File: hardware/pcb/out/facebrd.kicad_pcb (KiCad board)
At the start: 2 copper layers, 56 x 68 mm, 33 parts, among them J1 ToF 4P, J2 MIC pads, J3 EYES 6P, J4 BAT, J5 LED 3P, J6 AMP 5P, J7 TOUCH pads, J8 CHG, U1 XIAO-ESP32S3, U2 MPR121QR2, U3 MPU-6050

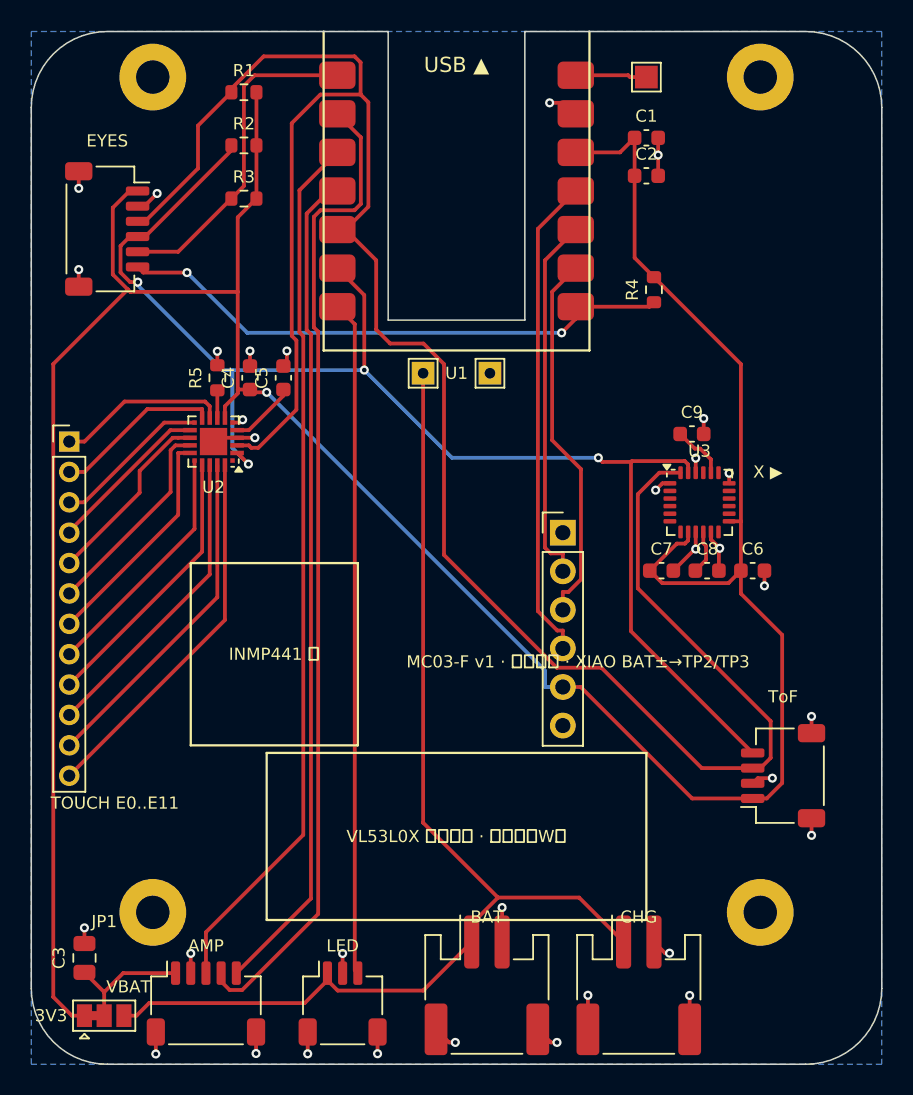
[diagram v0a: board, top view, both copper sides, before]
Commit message: pcb: correct MPR121 footprint (QFN-20 3x3 0.5 mm, 5 leads/side, no corner leads); local GND pour at U2
Co-Authored-By: Claude Fable 5.1 <noreply@anthropic.com>
Claude-Session: https://claude.ai/code/session_01F351BE8WNbsDJxZJegnrAN
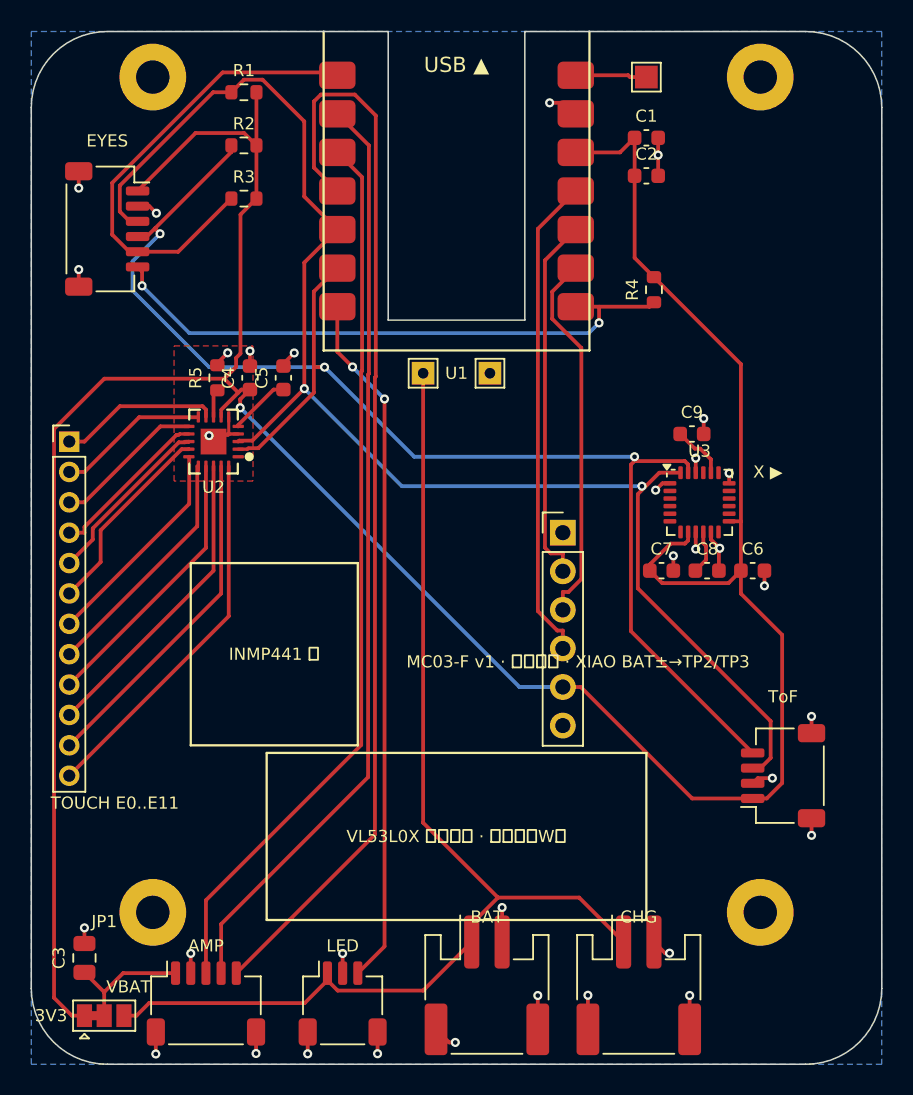
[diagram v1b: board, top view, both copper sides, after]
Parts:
- U2: footprint SiliconLabs_QFN-20-1EP_3x3mm_P0.5mm_EP1.8x1.8mm -> MC03:QFN-20_3x3_P0.5_MPR121
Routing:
- net SDA0: track 140.2 -> 95.5 mm, vias 0 -> 2
- net I2S_DIN: track 54.8 -> 71.6 mm
- net SDA1: track 21.8 -> 31.1 mm
- net I2S_LRC: track 65.3 -> 61.5 mm
- net SCL1: track 37.1 -> 39.4 mm
- net 3V3: track 198.9 -> 196.8 mm
- net SCL0: track 92.9 -> 94.6 mm, vias 4 -> 3
- net LED_DIN: track 44.4 -> 45.9 mm, vias 0 -> 2
- net I2S_BCLK: track 57.8 -> 59.0 mm
- net ELE1: track 11.1 -> 10.0 mm
- net GND: track 50.1 -> 49.3 mm
- net ELE0: track 11.2 -> 10.5 mm
- net ELE6: track 15.0 -> 14.3 mm
- net ELE4: track 12.2 -> 11.6 mm
- net ELE5: track 13.6 -> 13.0 mm
- added copper zone on F.Cu, net GND

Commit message: pcb: MPR121 pin map corrected against datasheet/KiCad symbol (7 REXT, 8-19 ELE, 20 VDD); MPU RESV pins NC; EP without paste
Co-Authored-By: Claude Fable 5.1 <noreply@anthropic.com>
Claude-Session: https://claude.ai/code/session_01F351BE8WNbsDJxZJegnrAN
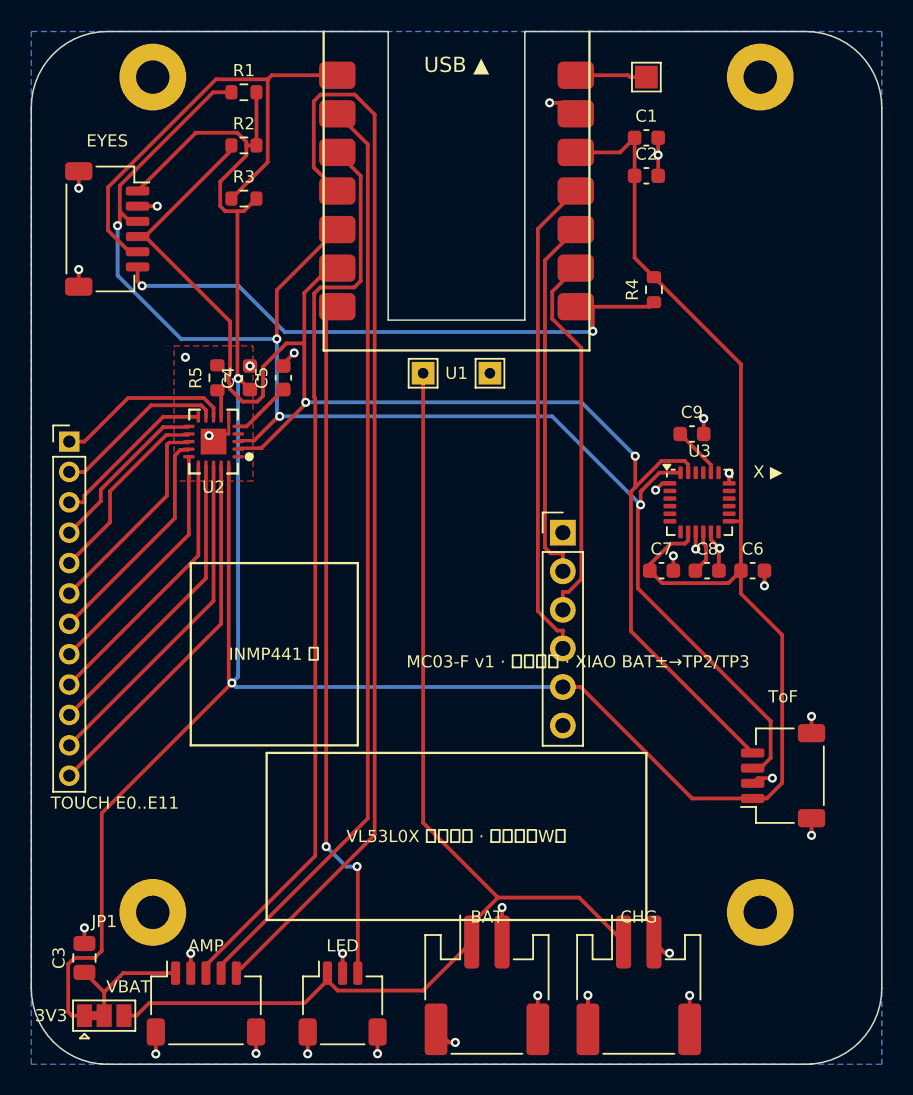
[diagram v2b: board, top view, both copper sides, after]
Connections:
- U2 pad 10: ELE1 -> ELE2
- U2 pad 11: ELE2 -> ELE3
- U2 pad 12: ELE3 -> ELE4
- U2 pad 13: ELE4 -> ELE5
- U2 pad 14: ELE5 -> ELE6
- U2 pad 15: ELE6 -> ELE7
- U2 pad 16: ELE7 -> ELE8
- U2 pad 17: ELE8 -> ELE9
- U2 pad 18: ELE9 -> ELE10
- U2 pad 19: ELE10 -> ELE11
- U2 pad 20: ELE11 -> 3V3
- U2 pad 7: 3V3 -> REXT
- U2 pad 8: REXT -> ELE0
- U2 pad 9: ELE0 -> ELE1
- U3 pad 22: GND -> (no net)
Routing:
- net GND: track 49.3 -> 44.3 mm, vias 33 -> 32
- net SDA0: track 95.5 -> 99.0 mm, vias 2 -> 4
- net SCL0: track 94.6 -> 96.2 mm, vias 3 -> 2
- net ELE1: track 10.0 -> 11.4 mm
- net I2S_BCLK: track 59.0 -> 60.3 mm
- net SDA1: track 31.1 -> 32.4 mm
- net ELE2: track 9.95 -> 11.1 mm
- net 3V3: track 196.8 -> 197.9 mm, vias 1 -> 2
- net ELE0: track 10.5 -> 11.6 mm
- net ELE4: track 11.6 -> 12.6 mm
- net ELE5: track 13.0 -> 14.0 mm
- net ELE6: track 14.3 -> 15.1 mm

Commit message: pcb: MPR121 on KiCad's own UQFN-20 3x3 0.4 mm footprint (no EP); 0.2 mm tracks / 0.13 clearance to escape it
Co-Authored-By: Claude Opus 5.5 <noreply@anthropic.com>
Claude-Session: https://claude.ai/code/session_01F351BE8WNbsDJxZJegnrAN
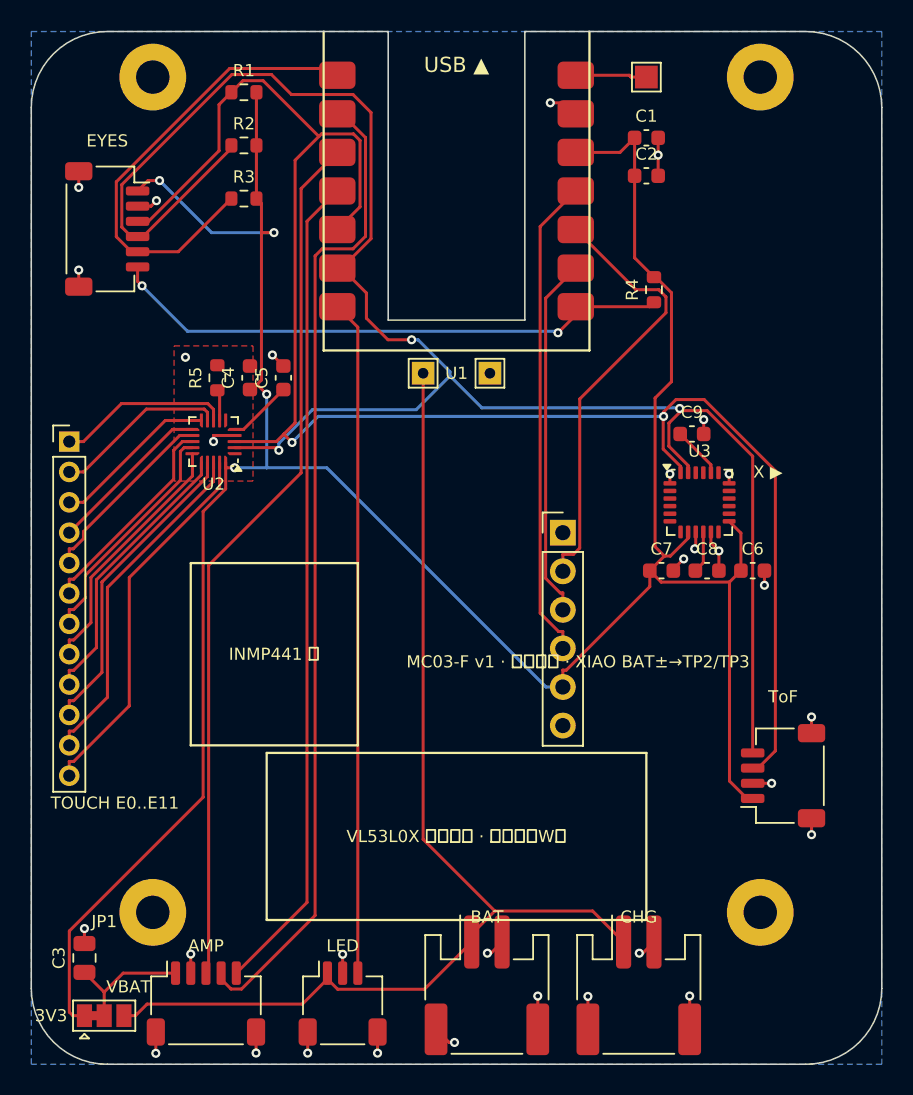
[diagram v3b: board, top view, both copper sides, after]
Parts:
- U2: footprint MC03:QFN-20_3x3_P0.5_MPR121 -> UQFN-20_3x3mm_P0.4mm
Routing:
- net SCL0: track 96.2 -> 119.0 mm, vias 2 -> 3
- net 3V3: track 197.9 -> 179.9 mm, vias 2 -> 4
- net I2S_DIN: track 71.6 -> 54.3 mm
- net SDA0: track 99.0 -> 113.0 mm, vias 4 -> 2
- net MIC_WS: track 24.3 -> 29.1 mm
- net I2S_LRC: track 61.4 -> 65.1 mm
- net I2S_BCLK: track 60.3 -> 57.6 mm
- net GND: track 44.3 -> 42.1 mm, vias 32 -> 31
- net SCL1: track 39.2 -> 37.5 mm
- net SDA1: track 32.4 -> 30.9 mm
- net LED_DIN: track 45.5 -> 44.4 mm, vias 2 -> 0
- net MIC_SCK: track 24.7 -> 23.9 mm
